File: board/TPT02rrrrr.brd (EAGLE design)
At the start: 28.4 x 28.4 mm, 16 parts, among them SW4 SW_SLIDECUS12B, U1 MOD_CYBLE014008-00, U2 REG_TPS61221

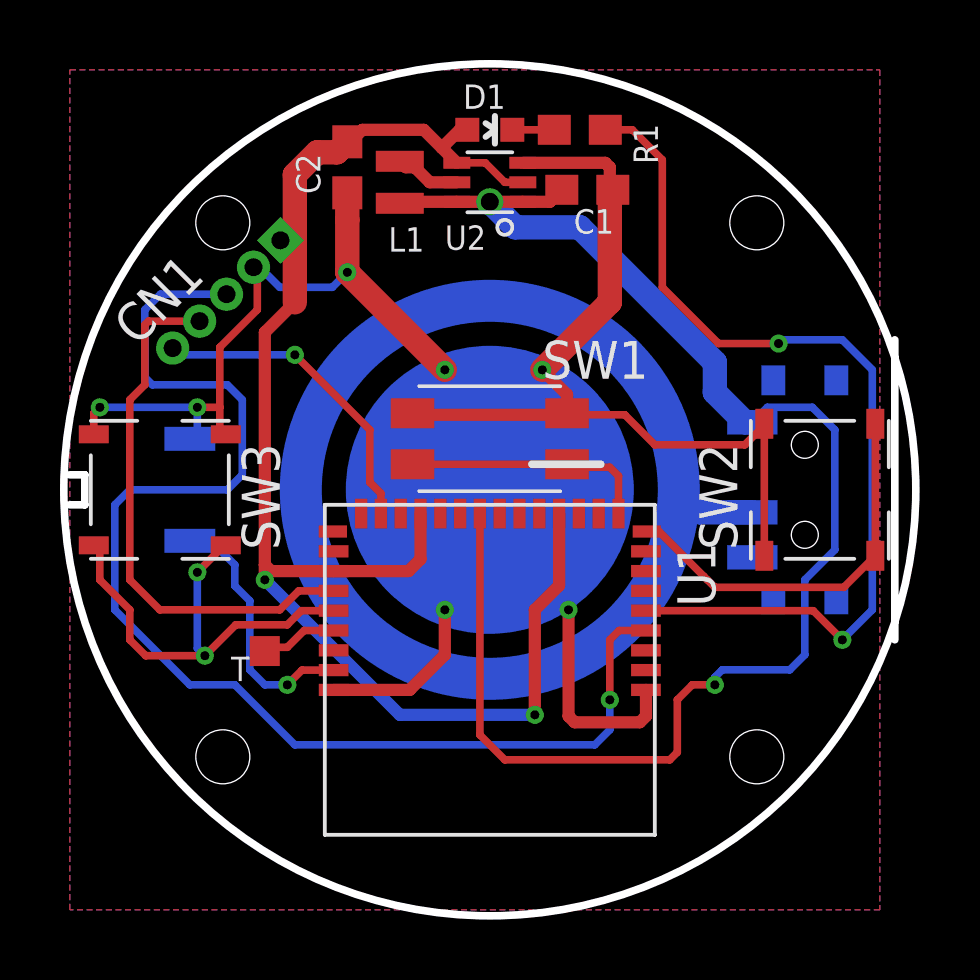
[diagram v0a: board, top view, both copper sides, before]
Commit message: 基板外径・シルクの微調整
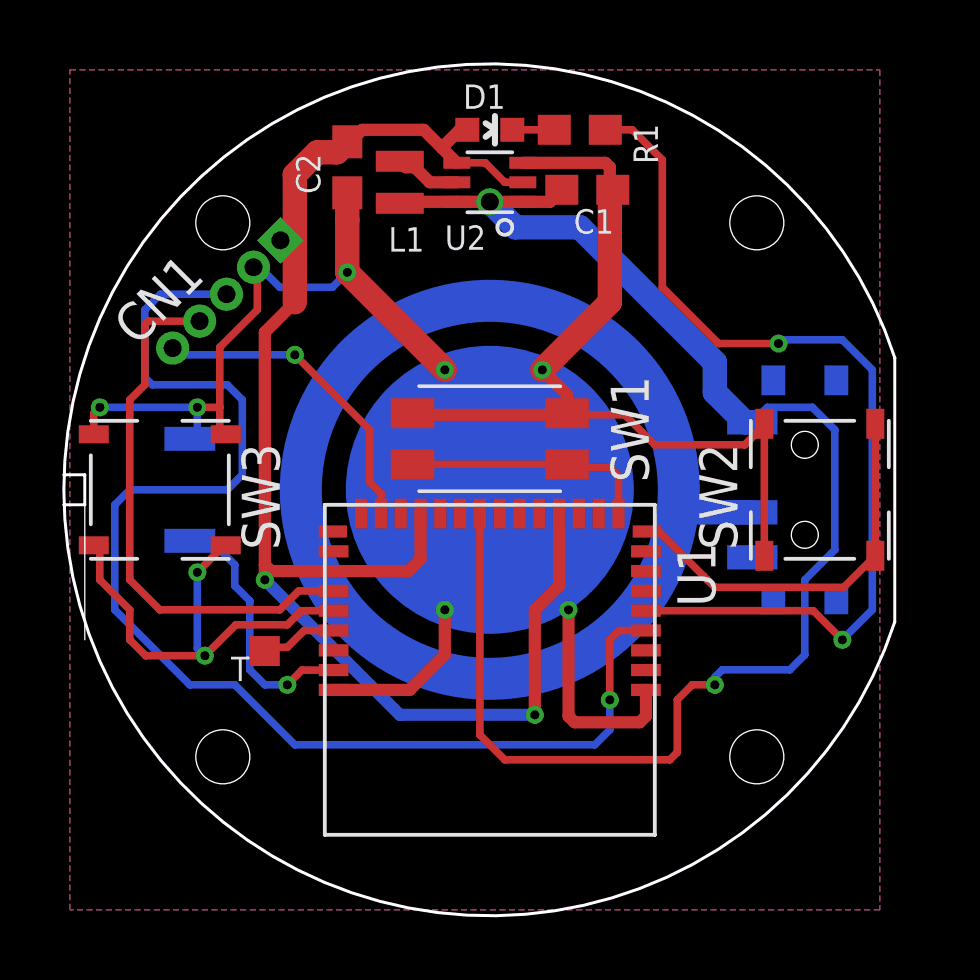
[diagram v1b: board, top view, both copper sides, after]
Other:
- board size 28.4 x 28.4 mm -> 27.7 x 28.4 mm
- board text added: "FnPresenterBLE v1.4"
- board text removed: "FnPresenterBLE v1.3"
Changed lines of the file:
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@@
 <grid distance="1" unitdist="mm" unit="mm" style="lines" multiple="1" display="yes" altdistance="0.25" altunitdist="mm" altunit="mm"/>
 <layers>
-<layer number="1" name="Top" color="4" fill="1" visible="yes" active="yes"/>
+<layer number="1" name="Top" color="4" fill="1" visible="no" active="yes"/>
 <layer number="16" name="Bottom" color="1" fill="1" visible="yes" active="yes"/>
 <layer number="17" name="Pads" color="2" fill="1" visible="yes" active="yes"/>
@@
 <layer number="19" name="Unrouted" color="6" fill="1" visible="yes" active="yes"/>
 <layer number="20" name="Dimension" color="15" fill="1" visible="yes" active="yes"/>
-<layer number="21" name="tPlace" color="7" fill="1" visible="yes" active="yes"/>
+<layer number="21" name="tPlace" color="7" fill="1" visible="no" active="yes"/>
 <layer number="22" name="bPlace" color="7" fill="1" visible="yes" active="yes"/>
-<layer number="23" name="tOrigins" color="15" fill="1" visible="yes" active="yes"/>
+<layer number="23" name="tOrigins" color="15" fill="1" visible="no" active="yes"/>
 <layer number="24" name="bOrigins" color="15" fill="1" visible="yes" active="yes"/>
-<layer number="25" name="tNames" color="7" fill="1" visible="yes" active="yes"/>
+<layer number="25" name="tNames" color="7" fill="1" visible="no" active="yes"/>
 <layer number="26" name="bNames" color="7" fill="1" visible="yes" active="yes"/>
 <layer number="27" name="tValues" color="7" fill="1" visible="no" active="yes"/>
@@
 <board>
 <plain>
-<circle x="15" y="15" radius="14.2" width="0.254" layer="20"/>
+<circle x="15" y="15" radius="14.2" width="0.01" layer="48"/>
 <circle x="15" y="15" radius="6.3" width="1.4" layer="16"/>
 <circle x="15" y="15" radius="4.8" width="0" layer="16"/>
@@
 <wire x1="21.75" y1="21.75" x2="8.25" y2="21.75" width="0.1" layer="48"/>
 <wire x1="8.25" y1="21.75" x2="8.25" y2="6.7" width="0.1" layer="48"/>
-<wire x1="28.5" y1="20" x2="28.5" y2="10" width="0.254" layer="20"/>
-<wire x1="1" y1="15.5" x2="1.5" y2="15.5" width="0.254" layer="20"/>
-<wire x1="1.5" y1="15.5" x2="1.5" y2="14.5" width="0.254" layer="20"/>
-<wire x1="1.5" y1="14.5" x2="1" y2="14.5" width="0.254" layer="20"/>
+<wire x1="28.5" y1="19.4" x2="28.5" y2="10.6" width="0.01" layer="48"/>
+<wire x1="0.8" y1="15.5" x2="1.5" y2="15.5" width="0.1" layer="20"/>
+<wire x1="1.5" y1="15.5" x2="1.5" y2="14.5" width="0.1" layer="20"/>
+<wire x1="1.5" y1="14.5" x2="0.8" y2="14.5" width="0.1" layer="20"/>
 <text x="21.5" y="3" size="1.27" layer="22" rot="MR0">FnPresenterBLE
-v1.3</text>
+v1.4</text>
 <text x="16.5" y="3" size="1.27" layer="22" rot="MR0">@akita11</text>
 <text x="23.5" y="17" size="0.8128" layer="26" rot="MR270">SW4</text>
-<wire x1="16.4" y1="15.85" x2="18.7" y2="15.85" width="0.254" layer="21"/>
 <wire x1="9" y1="24" x2="21" y2="24" width="0.254" layer="48"/>
 <wire x1="9" y1="21" x2="21" y2="21" width="0.254" layer="48"/>
+<wire x1="1.5" y1="14.5" x2="1.5" y2="10" width="0.01" layer="20"/>
+<wire x1="28.5" y1="10.6" x2="28.5" y2="19.4" width="0.1" layer="20" curve="-323.895736"/>
+<wire x1="28.5" y1="10.6" x2="28.5" y2="19.4" width="0.1" layer="20"/>
 </plain>
 <attributes>
@@
 <element name="CNM" library="akita" package="PAD_SMD1MM" value="CON_P01SMD1MM" x="15" y="15" smashed="yes" rot="MR0"/>
 <element name="SW1" library="akita" package="SW_EVQP2" value="" x="15" y="16.7" smashed="yes" rot="R180">
-<attribute name="NAME" x="16.75" y="18.7" size="1.27" layer="25"/>
+<attribute name="NAME" x="20.3" y="15.25" size="1.27" layer="25" rot="R90"/>
 <attribute name="VALUE" x="17.5" y="19.7" size="1.27" layer="27" rot="R180"/>
 </element>
